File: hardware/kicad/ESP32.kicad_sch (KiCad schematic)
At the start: 2 parts, among them J5 Screw_Terminal_01x19, J6 Screw_Terminal_01x19

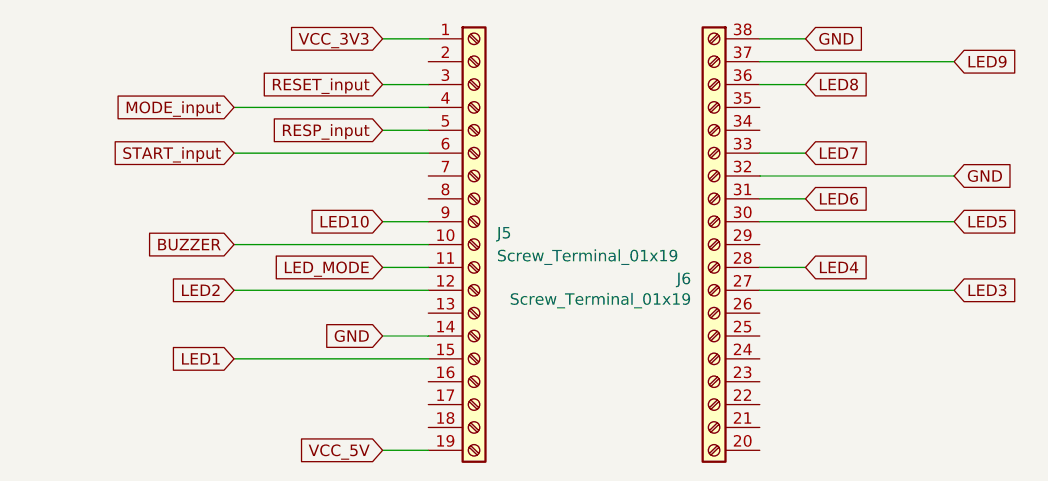
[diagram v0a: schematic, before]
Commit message: KiCad v0.2: pinout ESP32 DevKit 30 pines, botones con pull-up interna, buzzer a 5 V, resistencias SMD, logo
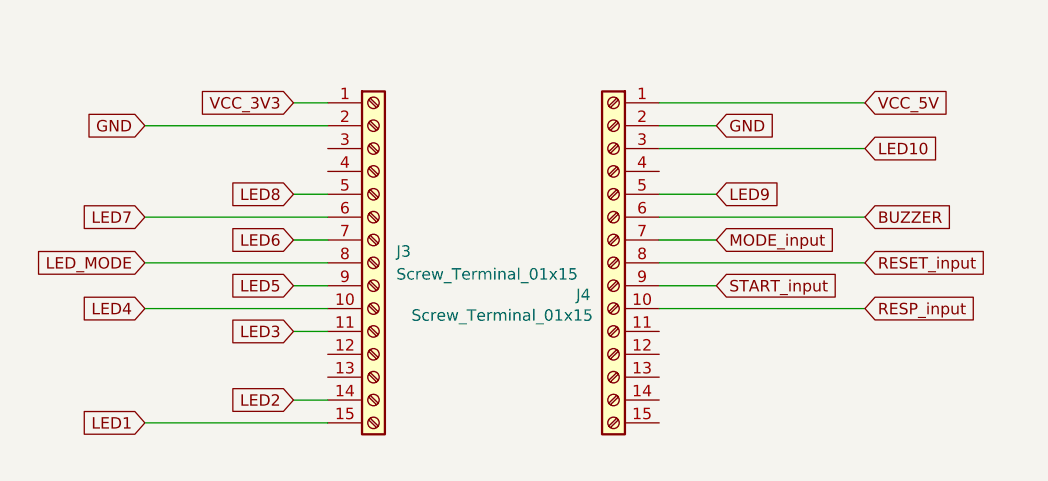
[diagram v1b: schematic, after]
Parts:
- removed J5, J6: Screw_Terminal_01x19, Connector_PinHeader_2.54mm:PinHeader_1x19_P2.54mm_Vertical, symbol Connector:Screw_Terminal_01x19
- added J3, J4: Screw_Terminal_01x15, Connector_PinHeader_2.54mm:PinHeader_1x15_P2.54mm_Vertical, symbol Connector:Screw_Terminal_01x15
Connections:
- net BUZZER: now also J4.6 (Pin_6)
- net GND: now also J3.2 (Pin_2), J4.2 (Pin_2)
- net LED1: now also J3.15 (Pin_15)
- net LED10: now also J4.3 (Pin_3)
- net LED2: now also J3.14 (Pin_14)
- net LED3: now also J3.11 (Pin_11)
- net LED4: now also J3.10 (Pin_10)
- net LED5: now also J3.9 (Pin_9)
- net LED6: now also J3.7 (Pin_7)
- net LED7: now also J3.6 (Pin_6)
- net LED8: now also J3.5 (Pin_5)
- net LED9: now also J4.5 (Pin_5)
- net LED_MODE: now also J3.8 (Pin_8)
- net MODE_input: now also J4.7 (Pin_7)
- net RESET_input: now also J4.8 (Pin_8)
- net RESP_input: now also J4.10 (Pin_10)
- net START_input: now also J4.9 (Pin_9)
- net VCC_3V3: now also J3.1 (Pin_1)
- net VCC_5V: now also J4.1 (Pin_1)
